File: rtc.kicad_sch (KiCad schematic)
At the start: 0 parts

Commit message: Power Section done + added backup lipo
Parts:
- added BT1: CR1220, symbol Device:Battery_Cell
- added C10: 10U, symbol Device:C
- added C9: 0.1U, symbol Device:C
- added R3, R4: R, symbol Device:R
- added U3: DS3231M, Package_SO:SOIC-16W_7.5x10.3mm_P1.27mm, symbol Timer_RTC:DS3231M
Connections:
- new net: BT1.1 (+), U3.14 (VBAT)
- new net +3.3V: C10.1, C9.1, R3.1, R4.1, U3.2 (VCC)
- new net 32KHZ: U3.1 (32KHZ)
- new net GND: BT1.2 (-), C10.2, C9.2, U3.10 (GND), U3.11 (GND), U3.12 (GND), U3.13 (GND), U3.5 (GND), U3.6 (GND), U3.7 (GND), U3.8 (GND), U3.9 (GND)
- new net RTC_RESET: U3.4 (~{RST})
- new net SCL: R4.2, U3.16 (SCL)
- new net SDA: R3.2, U3.15 (SDA)
- new net SQW: U3.3 (~{INT}/SQW)
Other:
- note added: "RTC"

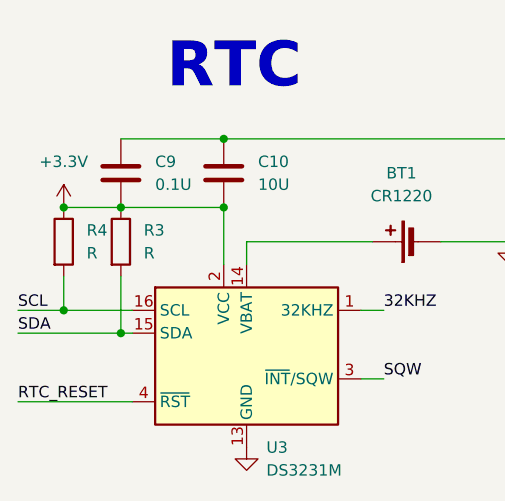
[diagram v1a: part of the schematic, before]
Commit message: fixed R values
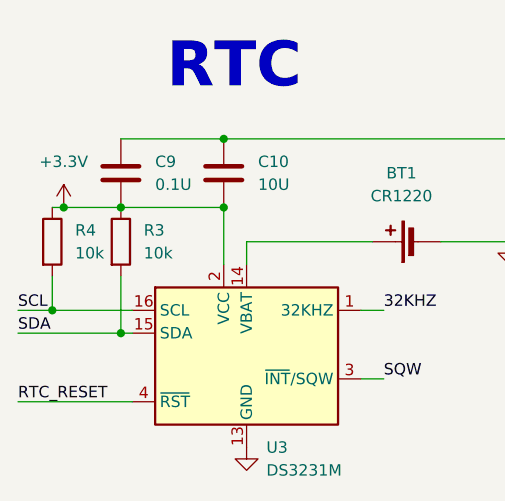
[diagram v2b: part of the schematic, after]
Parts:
- R3, R4: value R -> 10k
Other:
- moved on the sheet: R4
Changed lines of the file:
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@@
   (junction (at 125.73 81.28) (diameter 0) (color 0 0 0 0)
   )
+  (junction (at 124.46 92.71) (diameter 0) (color 0 0 0 0)
+  )
   (junction (at 175.26 85.09) (diameter 0) (color 0 0 0 0)
   )
@@
   (junction (at 132.08 95.25) (diameter 0) (color 0 0 0 0)
   )
-  (junction (at 125.73 92.71) (diameter 0) (color 0 0 0 0)
-  )
-  (wire (pts (xy 120.65 92.71) (xy 125.73 92.71))
+  (wire (pts (xy 120.65 92.71) (xy 124.46 92.71))
     (stroke (width 0) (type default))
   )
@@
     (stroke (width 0) (type default))
   )
-  (wire (pts (xy 125.73 88.9) (xy 125.73 92.71))
+  (wire (pts (xy 124.46 88.9) (xy 124.46 92.71))
     (stroke (width 0) (type default))
   )
@@
     (stroke (width 0) (type default))
   )
-  (wire (pts (xy 125.73 92.71) (xy 133.35 92.71))
+  (wire (pts (xy 124.46 92.71) (xy 133.35 92.71))
     (stroke (width 0) (type default))
   )
@@
   )
   (wire (pts (xy 175.26 73.66) (xy 175.26 85.09))
+    (stroke (width 0) (type default))
+  )
+  (wire (pts (xy 124.46 81.28) (xy 125.73 81.28))
     (stroke (width 0) (type default))
   )
@@
       (effects (font (size 1.27 1.27)) (justify left))
     )
-    (property "Value" "R" (at 134.62 86.36 0)
+    (property "Value" "10k" (at 134.62 86.36 0)
       (effects (font (size 1.27 1.27)) (justify left))
     )
@@
     )
   )
-  (symbol (lib_id "Device:R") (at 125.73 85.09 0) (unit 1)
-    (in_bom yes) (on_board yes) (dnp no) (fields_autoplaced)
-    (property "Reference" "R4" (at 128.27 83.82 0)
-      (effects (font (size 1.27 1.27)) (justify left))
-    )
-    (property "Value" "R" (at 128.27 86.36 0)
-      (effects (font (size 1.27 1.27)) (justify left))
-    )
-    (property "Footprint" "" (at 123.952 85.09 90)
-      (effects (font (size 1.27 1.27)) hide)
-    )
-    (property "Datasheet" "~" (at 125.73 85.09 0)
-      (effects (font (size 1.27 1.27)) hide)
-    )
+  (symbol (lib_id "Device:R") (at 124.46 85.09 0) (unit 1)
+    (in_bom yes) (on_board yes) (dnp no) (fields_autoplaced)
+    (property "Reference" "R4" (at 127 83.82 0)
+      (effects (font (size 1.27 1.27)) (justify left))
+    )
+    (property "Value" "10k" (at 127 86.36 0)
+      (effects (font (size 1.27 1.27)) (justify left))
+    )
+    (property "Footprint" "" (at 122.682 85.09 90)
+      (effects (font (size 1.27 1.27)) hide)
+    )
+    (property "Datasheet" "~" (at 124.46 85.09 0)
+      (effects (font (size 1.27 1.27)) hide)
+    )

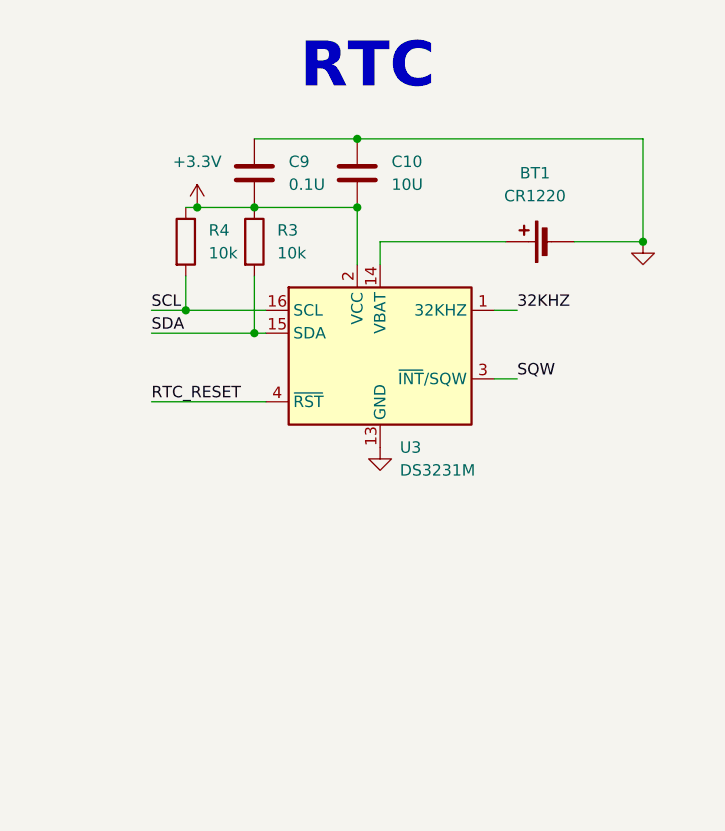
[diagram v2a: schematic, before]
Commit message: added io expander + rtc + fuel guage
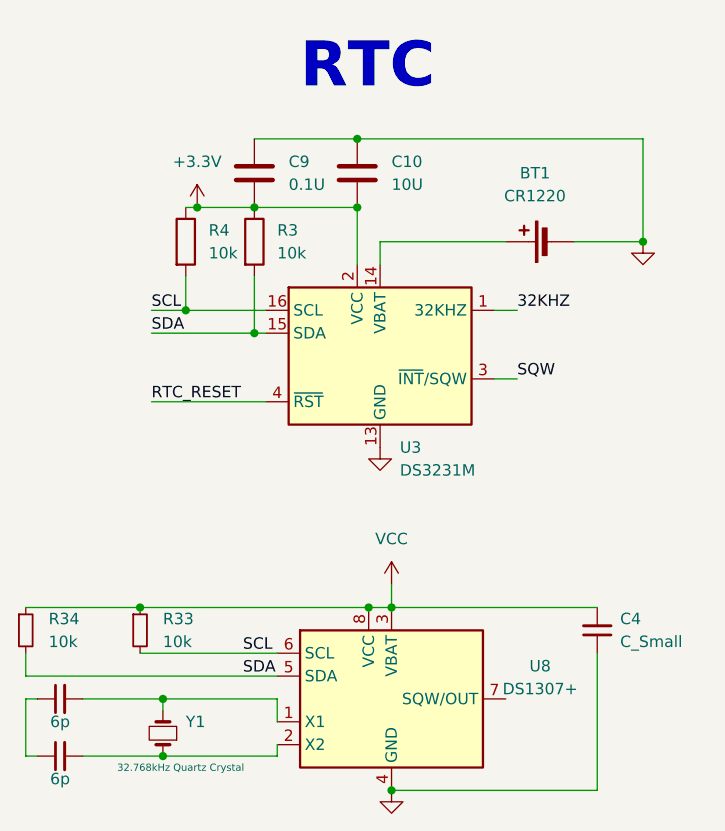
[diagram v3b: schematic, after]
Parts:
- added C11, C12: 6p, symbol Device:C_Small
- added C4: C_Small, symbol Device:C_Small
- added R33, R34: 10k, symbol Device:R_Small
- added U8: DS1307+, Package_DIP:DIP-8_W7.62mm, symbol Timer_RTC:DS1307+
- added Y1: 32.768kHz Quartz Crystal, symbol Device:Crystal_Small
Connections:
- net GND: now also C4.1, U8.4 (GND)
- net SCL: now also R33.2, U8.6 (SCL)
- net SDA: now also R34.2, U8.5 (SDA)
- new net: C12.2, U8.1 (X1), Y1.2
- new net: C11.2, U8.2 (X2), Y1.1
- new net: C11.1, C12.1
- new net VCC: C4.2, R33.1, R34.1, U8.3 (VBAT), U8.8 (VCC)
